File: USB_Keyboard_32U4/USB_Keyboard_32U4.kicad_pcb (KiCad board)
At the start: 2 copper layers, 15 x 35 mm, 14 parts, among them J1 USB_C_Receptacle_USB2.0_16P, J2 Conn_02x03_Odd_Even, U1 ATmega32U4-A, Y1 16mhz

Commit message: Update USB keyboard resistor value
Adjust the PCB resistor value from a generic `R` to `1k`, update the KiCad project layer state, and remove temporary lock files left behind during editing.
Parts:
- R7: value R -> 1k
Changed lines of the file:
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@@
 			)
 		)
-		(property "Value" "R"
+		(property "Value" "1k"
 			(at 0 -1.65 90)
 			(layer "B.Fab")

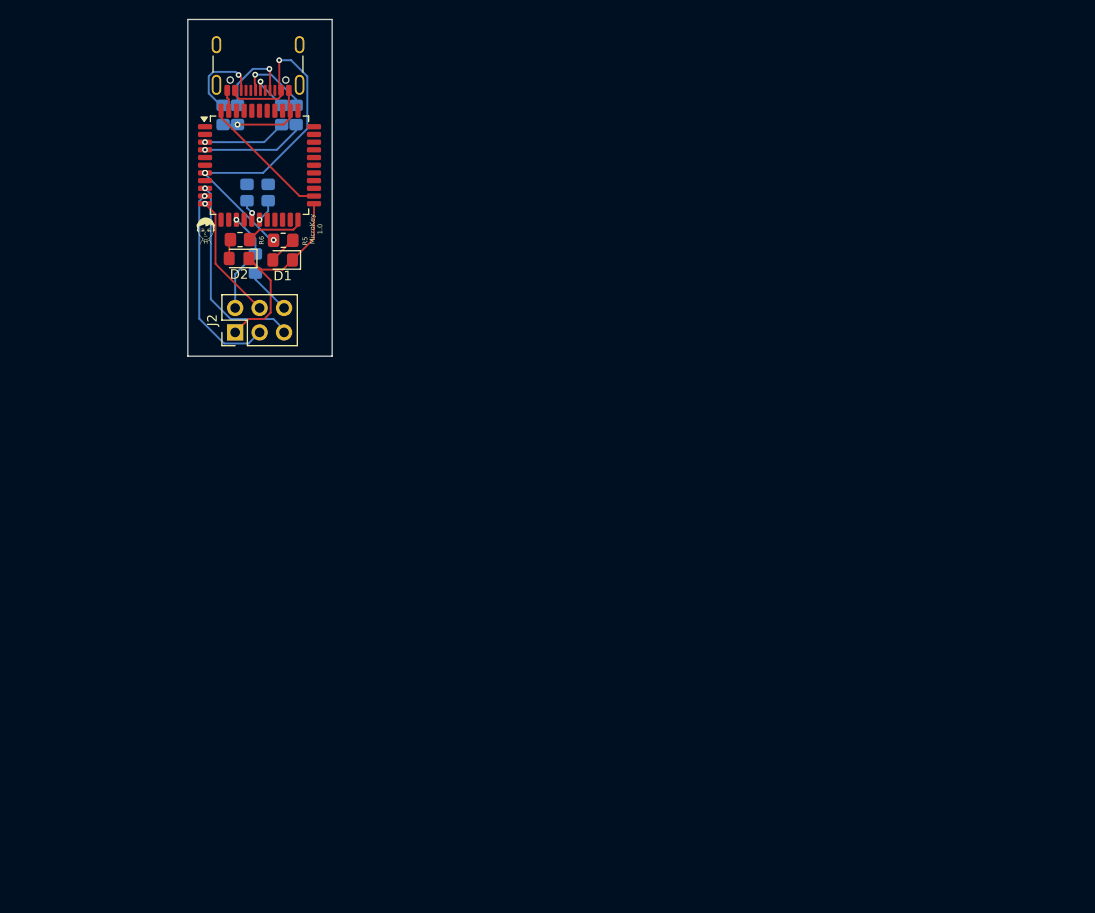
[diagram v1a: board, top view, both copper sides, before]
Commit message: Revise USB_Keyboard_32U4 PCB layout and footprints
Move and reorient many board footprints (ATmega32U4, USB-C J1, header J2, crystal Y1, LEDs/resistors) and update their pad rotations/layers. Replace/standardize several footprint definitions, adjust silkscreen/text orientations, update nets, routing (segments, vias) and Edge.Cuts arcs to match the new placement. Update project prefs (active_layer in .kicad_prl) and reorder used_designators in .kicad_pro. Add .kicad_pro lock file. These changes align footprints and routing with the revised physical layout.
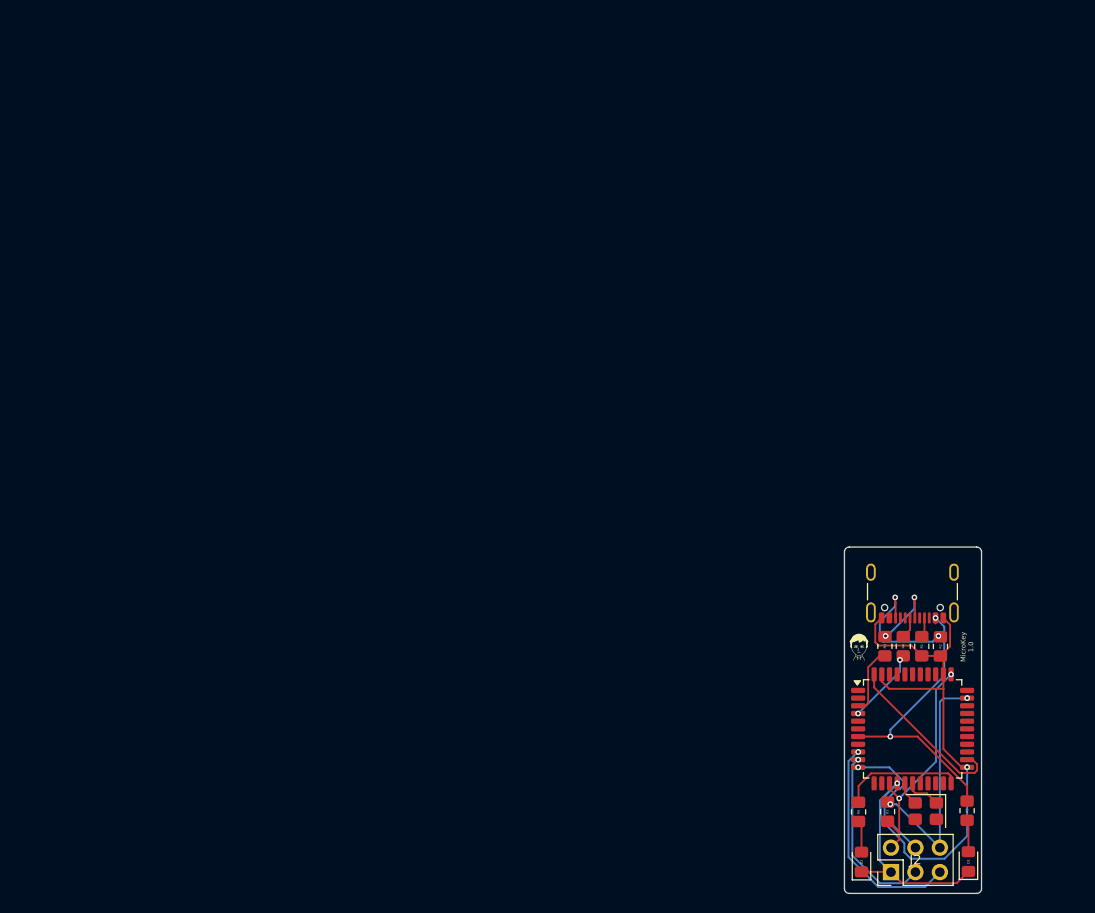
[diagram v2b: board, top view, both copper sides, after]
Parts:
- R1, R2, R3, R4, R7, Y1: moved to F.Cu
- moved D1 94.8 mm to (193.6, 153.8), turned to 90 degrees
- moved Y1 94.6 mm to (189.2, 148.5)
- moved R2 92.8 mm to (190.7, 131.4)
- moved R5 92.6 mm to (193.5, 148.5), turned to 90 degrees
- moved D2 90.1 mm to (182.5, 153.8), turned to 90 degrees
- moved R1 90.1 mm to (188.8, 131.4)
- moved U1 89.7 mm to (187.8, 140.0)
- moved J2 88.3 mm to (185.6, 154.9)
- moved R6 87.6 mm to (182.2, 148.6), turned to -90 degrees
- moved J1 87.4 mm to (187.8, 124.8)
- moved R7 87.0 mm to (185.2, 148.6), turned to -90 degrees
- moved R3 83.9 mm to (186.9, 131.4)
- moved R4 83.6 mm to (185.0, 131.4)
- moved G*** 80.5 mm to (182.3, 131.4)
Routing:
- net /Net-(J1-GND-PadA1): track 36.2 -> 81.7 mm, vias 1 -> 2
- net Net-(J2-Pin_6): track 4.86 -> 25.6 mm, vias 0 -> 2
- net Net-(J2-Pin_2): track 10.9 -> 24.3 mm, vias 1 -> 2
- net Net-(U1-VBUS): track 41.2 -> 30.6 mm, vias 4 -> 2
- net Net-(J1-CC1): track 8.50 -> 2.06 mm, vias 1 -> 0
- net /unconnected-(U1-PD5-Pad22): track 6.64 -> 12.7 mm
- net Net-(J1-D--PadA7): track 7.62 -> 2.24 mm, vias 1 -> 0
- net Net-(J1-CC2): track 8.97 -> 13.8 mm, vias 1 -> 2
- net Net-(U1-AVCC-Pad24): track 13.7 -> 17.7 mm
- net Net-(J1-D+-PadA6): track 4.38 -> 7.60 mm, vias 1 -> 2
- net Net-(U1-D+): track 10.9 -> 7.93 mm, vias 1 -> 2
- net Net-(J2-Pin_3): track 20.9 -> 18.5 mm, vias 2 -> 1
- net Net-(U1-D-): track 8.72 -> 7.09 mm, vias 1 -> 0
- net Net-(J2-Pin_5): track 21.3 -> 22.8 mm, vias 2 -> 1
- net Net-(U1-XTAL1): track 2.35 -> 3.74 mm, vias 1 -> 0
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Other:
- board size 15 x 35 mm -> 14.2 x 36 mm

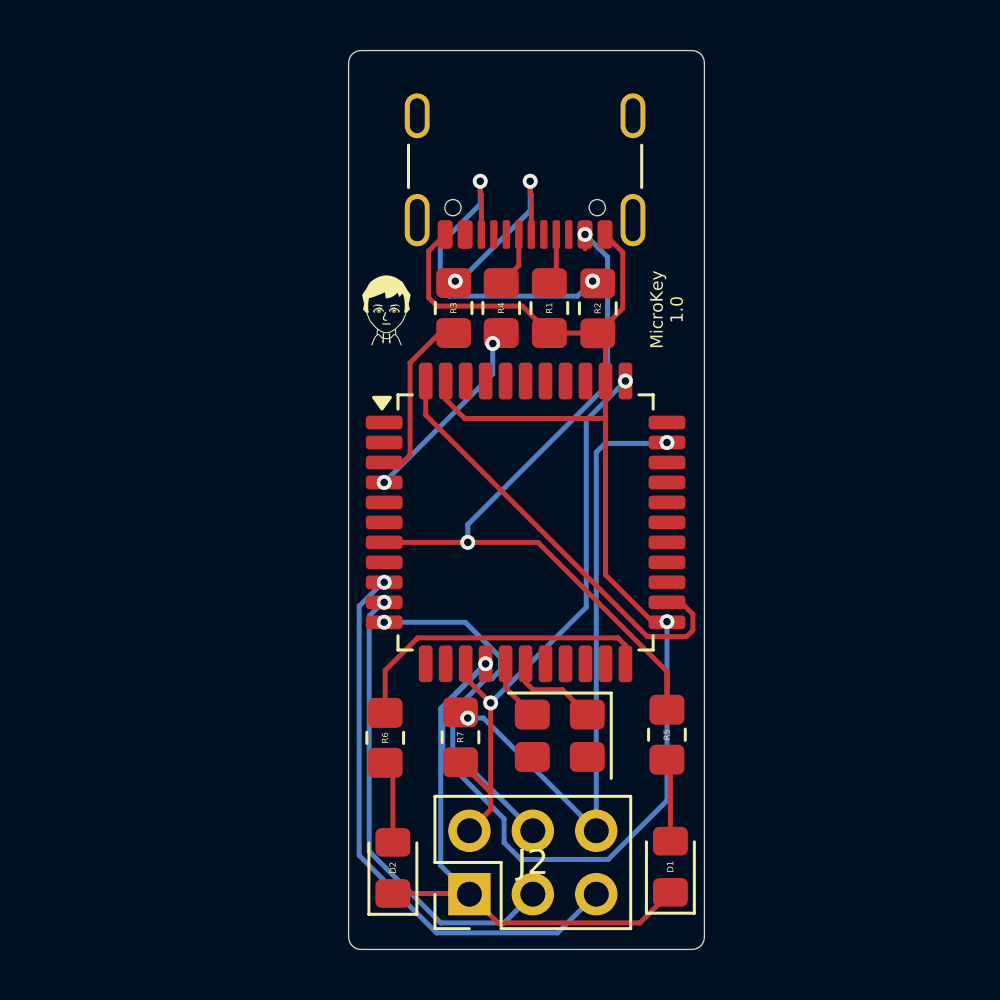
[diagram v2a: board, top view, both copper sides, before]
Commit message: Adjust PCB component placement
This commit updates the 32U4 keyboard PCB layout by repositioning and rotating key components, connectors, and USB-related footprints to match the revised board geometry. It also refreshes the associated silkscreen, edge-cut, and routing metadata while removing temporary KiCad lock files created during editing.
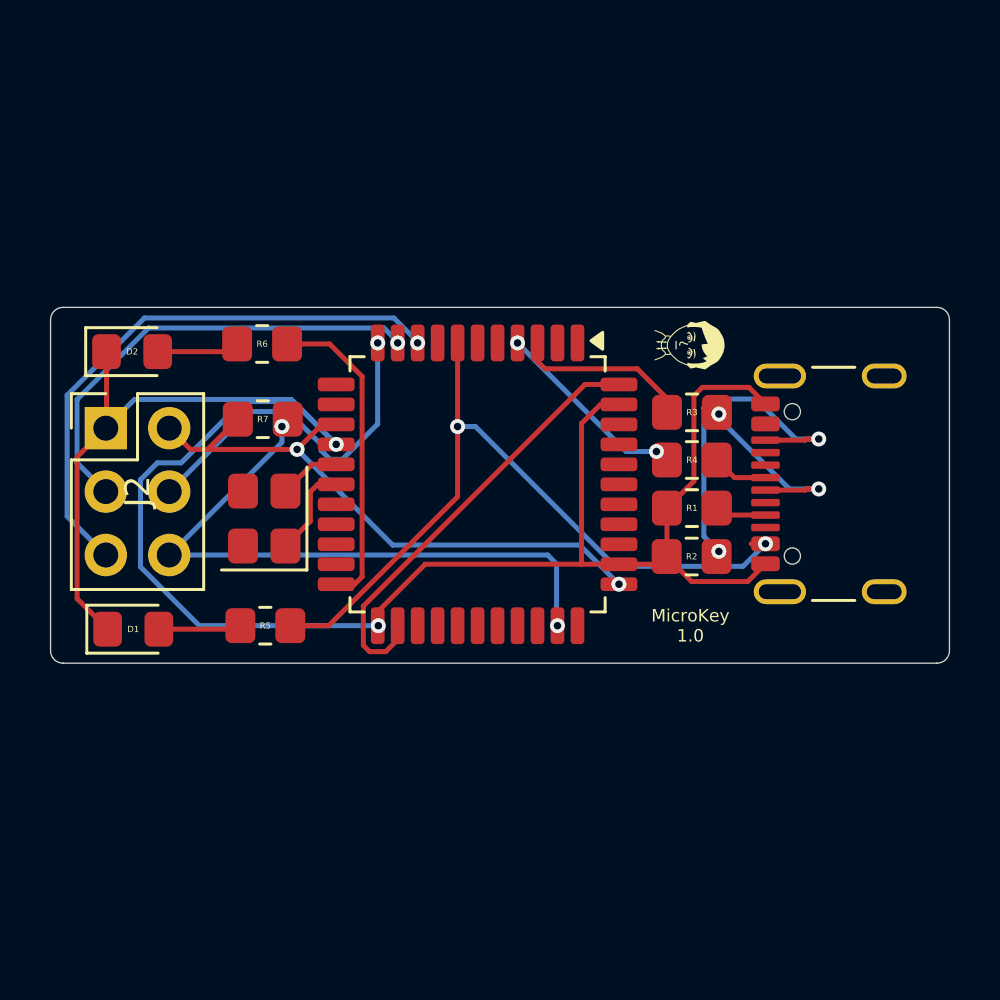
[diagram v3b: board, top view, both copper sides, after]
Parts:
- moved J2 23.7 mm to (171.0, 136.2), turned to 0 degrees
- moved D1 23.5 mm to (172.1, 144.3), turned to 0 degrees
- moved D2 23.2 mm to (172.1, 133.2), turned to 0 degrees
- moved J1 19.1 mm to (201.1, 138.5), turned to 90 degrees
- moved R5 16.7 mm to (177.4, 144.1), turned to 0 degrees
- moved R6 16.5 mm to (177.3, 132.9), turned to 180 degrees
- moved R7 15.0 mm to (177.3, 135.9), turned to 180 degrees
- moved Y1 14.7 mm to (177.4, 139.8), turned to 90 degrees
- moved G*** 12.3 mm to (194.5, 132.9), turned to -90 degrees
- moved R2 10.6 mm to (194.5, 141.4), turned to 180 degrees
- moved R4 10.4 mm to (194.5, 135.6), turned to 180 degrees
- moved R1 9.84 mm to (194.5, 139.4), turned to 180 degrees
- moved R3 9.76 mm to (194.5, 137.5), turned to 180 degrees
- moved U1 2.45 mm to (185.9, 138.5), turned to -90 degrees
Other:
- board size 14.2 x 36 mm -> 36 x 14.2 mm

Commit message: Updated schematic, pcb and bom.
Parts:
- removed the G*** at (194.5, 132.9)
- added C1: 27pF, Capacitor_SMD:C_0603_1608Metric_Pad1.08x0.95mm_HandSolder, F.Cu at (166.5, 146.8)
- added C2: 27pF, Capacitor_SMD:C_0603_1608Metric_Pad1.08x0.95mm_HandSolder, F.Cu at (160.6, 146.8)
- added C3: 100nF, Capacitor_SMD:C_0603_1608Metric_Pad1.08x0.95mm_HandSolder, F.Cu at (159.2, 127.6)
- added C4: 100nF, Capacitor_SMD:C_0603_1608Metric_Pad1.08x0.95mm_HandSolder, F.Cu at (158.1, 130.9)
- added C5: 100nF, Capacitor_SMD:C_0603_1608Metric_Pad1.08x0.95mm_HandSolder, F.Cu at (170.2, 131.1)
- added C6: 100nF, Capacitor_SMD:C_0603_1608Metric_Pad1.08x0.95mm_HandSolder, F.Cu at (169.5, 127.7)
- added C7: 10uF, Capacitor_SMD:C_0603_1608Metric_Pad1.08x0.95mm_HandSolder, F.Cu at (168.0, 127.7)
- added C8: 1uF, Capacitor_SMD:C_0603_1608Metric_Pad1.08x0.95mm_HandSolder, F.Cu at (156.7, 138.2)
- added C9: 100nF, Capacitor_SMD:C_0603_1608Metric_Pad1.08x0.95mm_HandSolder, F.Cu at (171.7, 136.7)
- added G***: LOGO, Custom Footprints:MIIImage 8.25mm, F.Cu at (171.3, 121.1)
- D1, D2: footprint LED_SMD:LED_0805_2012Metric_Pad1.15x1.40mm_HandSolder -> LED_SMD:LED_0603_1608Metric_Pad1.05x0.95mm_HandSolder
- J2: footprint Connector_PinHeader_2.54mm:PinHeader_2x03_P2.54mm_Vertical -> 2x3 Pads:MicroKey_AVR_ISP_2x3_SMD; moved to B.Cu
- R1, R2, R3, R4, R5, R6: footprint Resistor_SMD:R_0805_2012Metric_Pad1.20x1.40mm_HandSolder -> Resistor_SMD:R_0603_1608Metric_Pad0.98x0.95mm_HandSolder
- R7: value 1k -> 10k; footprint Resistor_SMD:R_0805_2012Metric_Pad1.20x1.40mm_HandSolder -> Resistor_SMD:R_0603_1608Metric_Pad0.98x0.95mm_HandSolder
- Y1: value 16mhz -> 16MHz
- moved J1 40.6 mm to (164.4, 121.0), turned to 180 degrees
- moved R2 36.0 mm to (161.2, 127.7), turned to -90 degrees
- moved R4 32.8 mm to (162.7, 127.7), turned to -90 degrees
- moved R3 31.9 mm to (164.2, 127.7), turned to -90 degrees
- moved R1 31.1 mm to (165.7, 127.7), turned to -90 degrees
- moved R6 22.6 mm to (156.7, 142.2), turned to -90 degrees
- moved U1 21.7 mm to (164.2, 137.7), turned to 0 degrees
- moved D2 18.4 mm to (157.7, 144.6), turned to 180 degrees
- moved Y1 15.5 mm to (163.6, 146.8), turned to 180 degrees
- moved J2 7.08 mm to (164.1, 137.6)
- moved R5 6.06 mm to (171.7, 142.2), turned to -90 degrees
- moved R7 4.83 mm to (173.7, 139.1), turned to 90 degrees
- moved D1 1.48 mm to (170.7, 144.7), turned to 180 degrees
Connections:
- net /unconnected-(U1-PD5-Pad22) renamed Net-(U1-PD5)
- net Net-(J2-Pin_3) renamed PB2
- net Net-(J2-Pin_4) renamed PB3
- net Net-(J2-Pin_5) renamed PB1
- D1 pad 1: /Net-(J1-GND-PadA1) -> Net-(D1-K)
- D1 pad 2: Net-(D1-A) -> GND
- D2 pad 1: /Net-(J1-GND-PadA1) -> GND
- J1 pad A1: /Net-(J1-GND-PadA1) -> GND
- J1 pad A12: /Net-(J1-GND-PadA1) -> GND
- J1 pad A4: Net-(U1-VBUS) -> VCC
- J1 pad A9: Net-(U1-VBUS) -> VCC
- J1 pad B1: /Net-(J1-GND-PadA1) -> GND
- J1 pad B12: /Net-(J1-GND-PadA1) -> GND
- J1 pad B4: Net-(U1-VBUS) -> VCC
- J1 pad B6: unconnected-(J1-D+-PadB6) -> Net-(J1-D+-PadA6)
- J1 pad B7: unconnected-(J1-D--PadB7) -> Net-(J1-D--PadA7)
- J1 pad B9: Net-(U1-VBUS) -> VCC
- J1 pad SH: unconnected-(J1-SHIELD-PadSH) -> GND
- J2 pad 1: /Net-(J1-GND-PadA1) -> GND
- J2 pad 2: Net-(J2-Pin_2) -> VCC
- J2 pad 6: Net-(J2-Pin_6) -> RESET
- R1 pad 2: /Net-(J1-GND-PadA1) -> GND
- R2 pad 2: /Net-(J1-GND-PadA1) -> GND
- R3 pad 2: Net-(U1-D+) -> D-
- R4 pad 2: Net-(U1-D-) -> D+
- R5 pad 1: Net-(D1-A) -> VCC
- R5 pad 2: Net-(U1-VBUS) -> Net-(D1-K)
- R7 pad 1: Net-(J2-Pin_6) -> VCC
- R7 pad 2: Net-(J2-Pin_2) -> RESET
- U1 pad 13: unconnected-(U1-~{RESET}-Pad13) -> RESET
- U1 pad 14: Net-(J2-Pin_2) -> VCC
- U1 pad 15: /Net-(J1-GND-PadA1) -> GND
- U1 pad 2: unconnected-(U1-UVCC-Pad2) -> VCC
- U1 pad 23: /Net-(J1-GND-PadA1) -> GND
- U1 pad 24: Net-(U1-AVCC-Pad24) -> VCC
- U1 pad 3: Net-(U1-D-) -> D-
- U1 pad 32: Net-(J2-Pin_6) -> unconnected-(U1-PC7-Pad32)
- U1 pad 34: Net-(J2-Pin_2) -> VCC
- U1 pad 35: /Net-(J1-GND-PadA1) -> GND
- U1 pad 4: Net-(U1-D+) -> D+
- U1 pad 42: unconnected-(U1-AREF-Pad42) -> Net-(U1-AREF)
- U1 pad 43: /Net-(J1-GND-PadA1) -> GND
- U1 pad 44: Net-(U1-AVCC-Pad24) -> VCC
- U1 pad 5: unconnected-(U1-UGND-Pad5) -> GND
- U1 pad 6: unconnected-(U1-UCAP-Pad6) -> Net-(U1-UCAP)
- U1 pad 7: Net-(U1-VBUS) -> VCC
- Y1 pad 2: Net-(U1-XTAL2) -> GND
- Y1 pad 3: (no net) -> Net-(U1-XTAL2)
- Y1 pad 4: (no net) -> GND
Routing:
- net GND: track 0.00 -> 90.3 mm, vias 0 -> 7
- net /Net-(J1-GND-PadA1): track 81.7 -> 0.00 mm, vias 2 -> 0
- net VCC: track 0.00 -> 79.8 mm, vias 0 -> 4
- net Net-(U1-VBUS): track 30.6 -> 0.00 mm, vias 2 -> 0
- net Net-(J2-Pin_6): track 25.6 -> 0.00 mm, vias 2 -> 0
- net Net-(J2-Pin_2): track 24.3 -> 0.00 mm, vias 2 -> 0
- net RESET: track 0.00 -> 23.8 mm, vias 0 -> 2
- net Net-(U1-AREF): track 0.00 -> 19.1 mm, vias 0 -> 2
- net Net-(U1-AVCC-Pad24): track 17.7 -> 0.00 mm
- net PB1: track 22.8 -> 8.20 mm
- net D+: track 0.00 -> 12.8 mm, vias 0 -> 2
- net D-: track 0.00 -> 11.8 mm, vias 0 -> 2
- net PB2: track 18.5 -> 7.10 mm
- net Net-(J1-CC2): track 13.8 -> 2.71 mm, vias 2 -> 0
- net Net-(U1-XTAL2): track 2.48 -> 10.4 mm, vias 0 -> 2
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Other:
- board size 36 x 14.2 mm -> 23.1 x 33 mm
- board text added: "GND"
- board text added: "Liam Carlson"
- board text added: "Made in Canada"
- board text added: "Microkey 1.0"
- board text added: "PB1"
- board text added: "PB2"
- board text added: "PB3"
- board text added: "Reset"
- board text added: "VCC"

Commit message: Added a folder with finished files.
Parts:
- removed G***: LOGO, Custom Footprints:MIIImage 8.25mm
- J2: moved to F.Cu
- moved R7 71.5 mm to (107.6, 111.8), turned to 0 degrees
- moved J2 67.0 mm to (105.0, 106.0)
- moved C2 65.1 mm to (103.7, 115.0), turned to 0 degrees
- moved C1 64.2 mm to (107.5, 121.4), turned to 180 degrees
- moved Y1 64.0 mm to (106.4, 118.0), turned to 90 degrees
- moved C5 57.6 mm to (112.8, 126.0), turned to 180 degrees
- moved D2 55.5 mm to (105.0, 127.0), turned to 90 degrees
- moved R6 55.0 mm to (105.0, 123.5)
- moved C4 54.0 mm to (107.0, 113.5), turned to 180 degrees
- moved R5 53.5 mm to (128.2, 111.0)
- moved R2 53.2 mm to (112.0, 107.5), turned to 180 degrees
- moved D1 52.1 mm to (128.2, 114.5), turned to 90 degrees
- moved U1 52.1 mm to (116.0, 118.0), turned to -90 degrees
- moved C9 51.4 mm to (124.5, 116.4), turned to 0 degrees
- moved C8 51.2 mm to (113.7, 110.3), turned to 180 degrees
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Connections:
- D1 pad 1: Net-(D1-K) -> GND
- D1 pad 2: GND -> Net-(D1-A)
- R5 pad 2: Net-(D1-K) -> Net-(D1-A)
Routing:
- net GND: track 90.3 -> 13.1 mm, vias 7 -> 22
- net VCC: track 79.8 -> 97.6 mm, vias 4 -> 3
- net Net-(U1-AREF): track 19.1 -> 2.31 mm, vias 2 -> 0
- net RESET: track 23.8 -> 8.02 mm, vias 2 -> 0
- net PB1: track 8.20 -> 21.9 mm, vias 1 -> 0
- net D+: track 12.8 -> 2.26 mm, vias 2 -> 0
- net D-: track 11.8 -> 1.93 mm, vias 2 -> 0
- net PB2: track 7.10 -> 15.2 mm, vias 1 -> 0
- net PB3: track 16.7 -> 8.94 mm, vias 3 -> 0
- net Net-(U1-PD5): track 16.3 -> 8.62 mm
- net Net-(U1-XTAL2): track 10.4 -> 8.24 mm, vias 2 -> 0
- net Net-(U1-XTAL1): track 4.69 -> 6.53 mm
- net Net-(D1-A): track 0.00 -> 1.71 mm
- net Net-(J1-CC2): track 2.71 -> 4.35 mm
- net Net-(D1-K): track 1.62 -> 0.00 mm
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- added copper zone on B.Cu, net GND
- added copper zone on F.Cu, net GND
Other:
- board size 23.1 x 33 mm -> 31 x 33.5 mm
- board text added: "1"
- board text added: "2"
- board text added: "3"
- board text added: "4"
- board text added: "5"
- board text added: "6"
- board text removed: "GND"
- board text removed: "Liam Carlson"
- board text removed: "Made in Canada"
- board text removed: "MicroKey 1.0"
- board text removed: "Microkey 1.0"
- board text removed: "PB1"
- board text removed: "PB2"
- board text removed: "PB3"
- board text removed: "Reset"
- board text removed: "VCC"
